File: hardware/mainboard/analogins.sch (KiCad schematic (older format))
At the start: 24 parts, among them U13 MCP6004, U14 MCP6001-OT

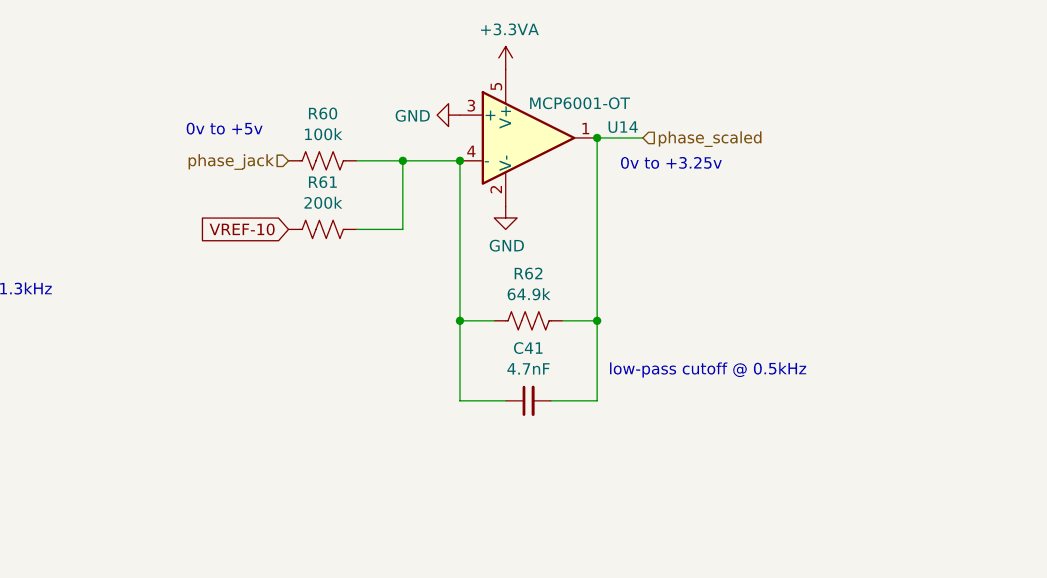
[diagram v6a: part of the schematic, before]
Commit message: Change phase in to hard sync button, remove unneeded parts, make v2 mainboard
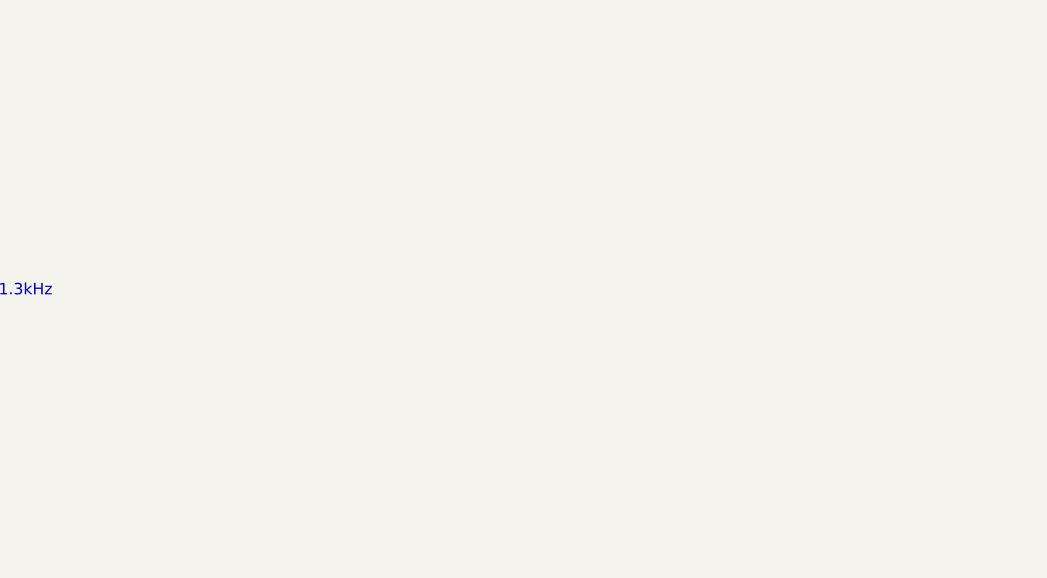
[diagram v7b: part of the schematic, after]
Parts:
- removed C41: 4.7nF, Capacitor_SMD:C_0603_1608Metric_Pad1.05x0.95mm_HandSolder, symbol Device:C_Small
- removed R60: 100k, Resistor_SMD:R_0603_1608Metric_Pad1.05x0.95mm_HandSolder, symbol Device:R_US
- removed R61: 200k, Resistor_SMD:R_0603_1608Metric_Pad1.05x0.95mm_HandSolder, symbol Device:R_US
- removed R62: 64.9k, Resistor_SMD:R_0603_1608Metric_Pad1.05x0.95mm_HandSolder, symbol Device:R_US
- removed U14: MCP6001-OT, Package_TO_SOT_SMD:SOT-23-5, symbol Amplifier_Operational:MCP6001-OT
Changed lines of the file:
@@
 Sheet 5 7
 Title "Castor & Pollux"
-Date "2020-09-07"
-Rev "v1"
+Date "2020-09-26"
+Rev "v2"
 Comp "Winterbloom"
 Comment1 "CC BY-SA 4.0"
@@
 duty_b_jack
 $Comp
-L Amplifier_Operational:MCP6001-OT U14
-U 1 1 5F381AB9
-P 5750 1200
-F 0 "U14" H 6094 1246 50  0000 L CNN
-F 1 "MCP6001-OT" H 5750 1350 50  0000 L CNN
-F 2 "Package_TO_SOT_SMD:SOT-23-5" H 5650 1000 50  0001 L CNN
-F 3 "http://ww1.microchip.com/downloads/en/DeviceDoc/21733j.pdf" H 5750 1400 50  0001 C CNN
-F 4 "yes" H 5750 1200 50  0001 C CNN "finalized"
-F 5 "MCP6001T-I/OT" H 5750 1200 50  0001 C CNN "mpn"
-	1    5750 1200
-	1    0    0    -1
-$EndComp
-$Comp
-L Device:R_US R60
-U 1 1 5F3849CF
-P 4850 1300
-F 0 "R60" V 4645 1300 50  0000 C CNN
-F 1 "100k" V 4736 1300 50  0000 C CNN
-F 2 "Resistor_SMD:R_0603_1608Metric_Pad1.05x0.95mm_HandSolder" V 4890 1290 50  0001 C CNN
-F 3 "~" H 4850 1300 50  0001 C CNN
-F 4 "yes" H 4850 1300 50  0001 C CNN "finalized"
-F 5 "ERA-3AED104V" H 4850 1300 50  0001 C CNN "mpn"
-F 6 "0.5%" H 4850 1300 50  0001 C CNN "Reqs"
-F 7 "100mW" H 4850 1300 50  0001 C CNN "mpn specs"
-	1    4850 1300
-	0    1    1    0
-$EndComp
-$Comp
-L Device:R_US R61
-U 1 1 5F3849D5
-P 4850 1600
-F 0 "R61" V 4645 1600 50  0000 C CNN
-F 1 "200k" V 4736 1600 50  0000 C CNN
-F 2 "Resistor_SMD:R_0603_1608Metric_Pad1.05x0.95mm_HandSolder" V 4890 1590 50  0001 C CNN
-F 3 "~" H 4850 1600 50  0001 C CNN
-F 4 "yes" H 4850 1600 50  0001 C CNN "finalized"
-F 5 "ERA-3AEB204V" H 4850 1600 50  0001 C CNN "mpn"
-F 6 "100mW" H 4850 1600 50  0001 C CNN "mpn specs"
-	1    4850 1600
-	0    1    1    0
-$EndComp
-$Comp
-L Device:R_US R62
-U 1 1 5F3849DB
-P 5750 2000
-F 0 "R62" V 5545 2000 50  0000 C CNN
-F 1 "64.9k" V 5636 2000 50  0000 C CNN
-F 2 "Resistor_SMD:R_0603_1608Metric_Pad1.05x0.95mm_HandSolder" V 5790 1990 50  0001 C CNN
-F 3 "~" H 5750 2000 50  0001 C CNN
-F 4 "yes" H 5750 2000 50  0001 C CNN "finalized"
-F 5 "ERA-3AEB6492V" H 5750 2000 50  0001 C CNN "mpn"
-F 6 "100mW" H 5750 2000 50  0001 C CNN "mpn specs"
-	1    5750 2000
-	0    1    1    0
-$EndComp
-$Comp
-L Device:C_Small C41
-U 1 1 5F3849E1
-P 5750 2350
-F 0 "C41" V 5979 2350 50  0000 C CNN
-F 1 "4.7nF" V 5888 2350 50  0000 C CNN
-F 2 "Capacitor_SMD:C_0603_1608Metric_Pad1.05x0.95mm_HandSolder" H 5750 2350 50  0001 C CNN
-F 3 "~" H 5750 2350 50  0001 C CNN
-F 4 "yes" H 5750 2350 50  0001 C CNN "finalized"
-F 5 "MF-CAP-0603-4.7nF" H 5750 2350 50  0001 C CNN "mpn"
-F 6 "10% 50v" H 5750 2350 50  0001 C CNN "mpn specs"
-F 7 "GCD188R71H472MA01D" H 5750 2350 50  0001 C CNN "mpn alt"
-	1    5750 2350
-	0    -1   -1   0
-$EndComp
-$Comp
-L power:GND #PWR0119
-U 1 1 5F3849E7
-P 5450 1100
-F 0 "#PWR0119" H 5450 850 50  0001 C CNN
-F 1 "GND" V 5455 972 50  0000 R CNN
-F 2 "" H 5450 1100 50  0001 C CNN
-F 3 "" H 5450 1100 50  0001 C CNN
-	1    5450 1100
-	0    1    1    0
-$EndComp
-Text HLabel 4700 1300 0    50   Input ~ 0
-phase_jack
-Text GLabel 4700 1600 0    50   Input ~ 0
-VREF-10
-Wire Wire Line
-	5450 2000 5600 2000
-Wire Wire Line
-	5900 2000 6050 2000
-Wire Wire Line
-	5650 2350 5450 2350
-Wire Wire Line
-	5450 2350 5450 2000
-Connection ~ 5450 2000
-Wire Wire Line
-	5850 2350 6050 2350
-Wire Wire Line
-	6050 2350 6050 2000
-Connection ~ 6050 2000
-Wire Wire Line
-	5000 1300 5200 1300
-Wire Wire Line
-	5000 1600 5200 1600
-Wire Wire Line
-	5200 1600 5200 1300
-Connection ~ 5200 1300
-Wire Wire Line
-	5200 1300 5450 1300
-Wire Wire Line
-	6050 1200 6250 1200
-Text HLabel 6250 1200 2    50   Input ~ 0
-phase_scaled
-Text Notes 6150 1350 0    50   ~ 0
-0v to +3.25v
-Text Notes 4250 1200 0    50   ~ 0
-0v to +5v
-$Comp
-L power:GND #PWR0120
-U 1 1 5F3905AF
-P 5650 1500
-F 0 "#PWR0120" H 5650 1250 50  0001 C CNN
-F 1 "GND" H 5655 1327 50  0000 C CNN
-F 2 "" H 5650 1500 50  0001 C CNN
-F 3 "" H 5650 1500 50  0001 C CNN
-	1    5650 1500
-	1    0    0    -1
-$EndComp
-Wire Wire Line
-	5450 1300 5450 2000
-Connection ~ 5450 1300
-Wire Wire Line
-	6050 1200 6050 2000
-Connection ~ 6050 1200
-$Comp
-L power:+3.3VA #PWR0121
-U 1 1 5F3951CD
-P 5650 900
-F 0 "#PWR0121" H 5650 750 50  0001 C CNN
-F 1 "+3.3VA" H 5665 1073 50  0000 C CNN
-F 2 "" H 5650 900 50  0001 C CNN
-F 3 "" H 5650 900 50  0001 C CNN
-	1    5650 900
-	1    0    0    -1
-$EndComp
-$Comp
 L Amplifier_Operational:MCP6004 U13
 U 5 1 5F395FB8
@@
 Text Notes 2750 6300 0    50   ~ 0
 low-pass cutoff @ 0.5kHz
-Text Notes 6100 2250 0    50   ~ 0
-low-pass cutoff @ 0.5kHz
 Text Notes 6700 6000 0    50   ~ 0
